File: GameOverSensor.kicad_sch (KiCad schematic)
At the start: 28 parts

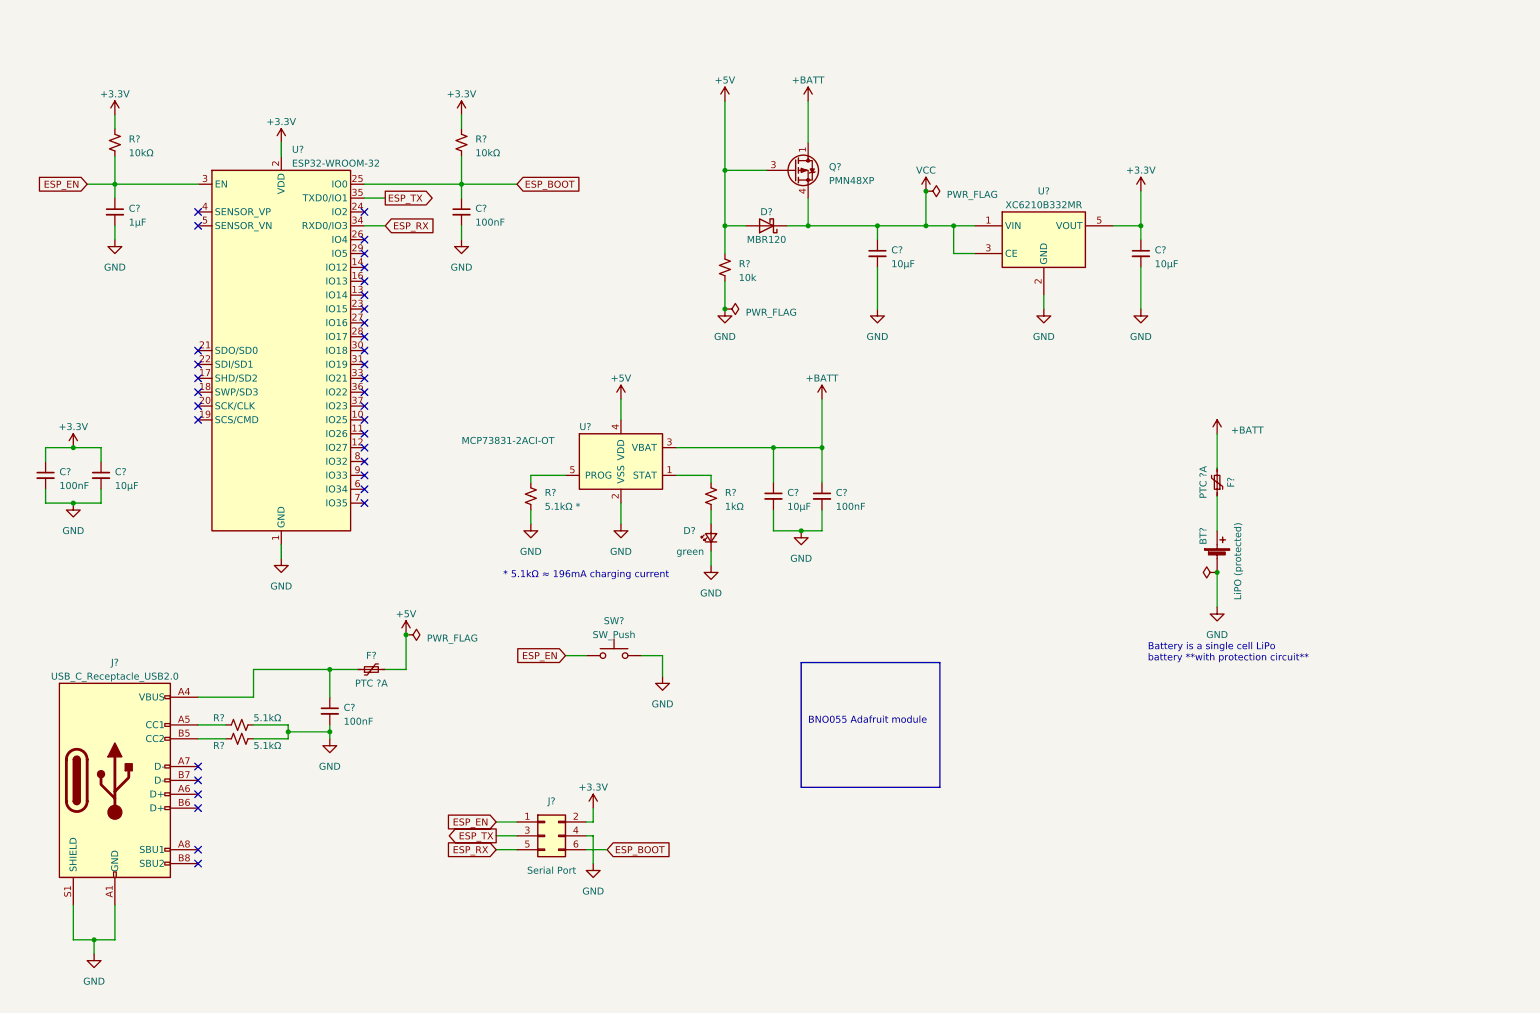
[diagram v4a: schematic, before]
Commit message: Reorganizes schematics a bit
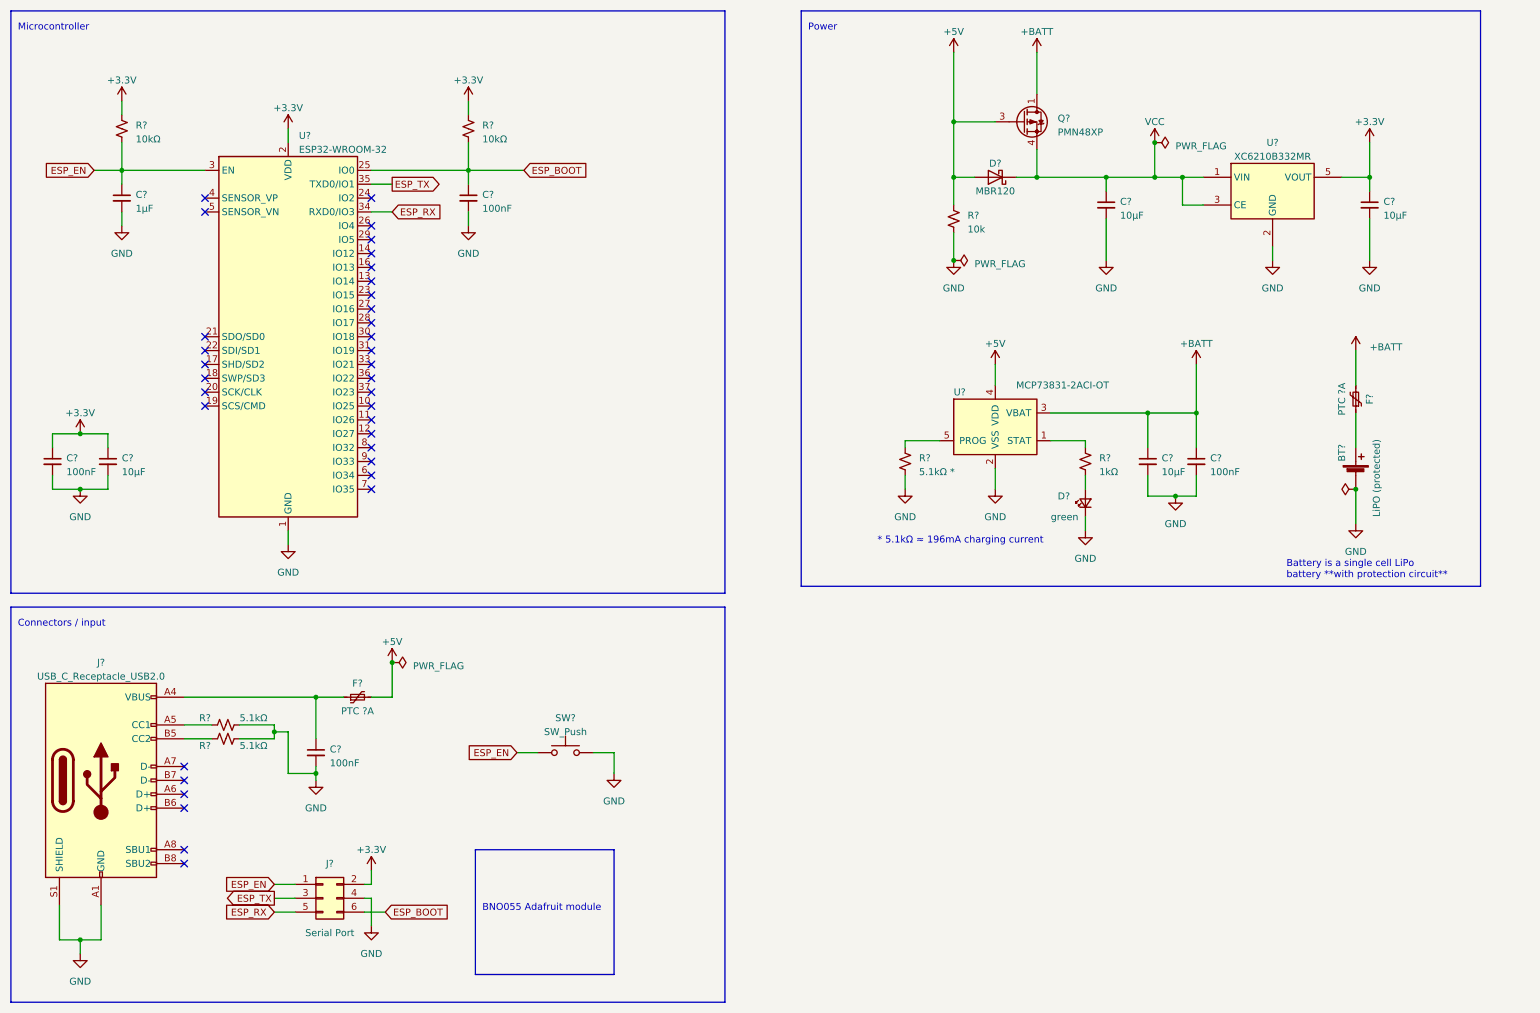
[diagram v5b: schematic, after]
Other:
- note added: "Connectors / input"
- note added: "Microcontroller"
- note added: "Power"
- company: (none) -> Dancelab Game Over
- title: (none) -> Game Over sensor
- moved on the sheet: BT?, C?, D?, F?, J?, Q?, R?, SW?, U?

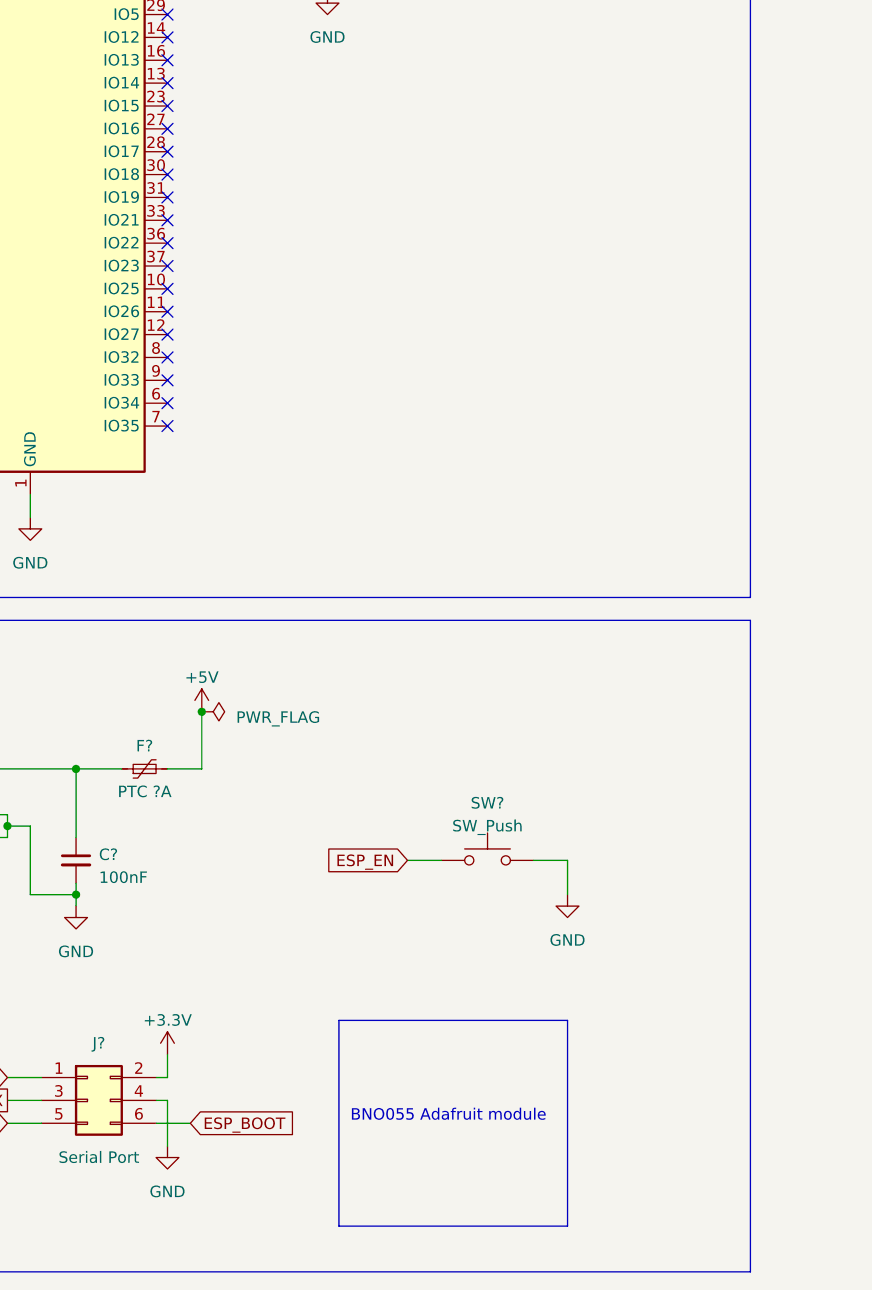
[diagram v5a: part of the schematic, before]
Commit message: Adds BON055 module symbol
We will use the Adafruit BON055 breakout board as we couldn't source the
BNO055 anywhere. This commit includes the schematic symbol but we still
need to make the footprint to be included in the PCB.
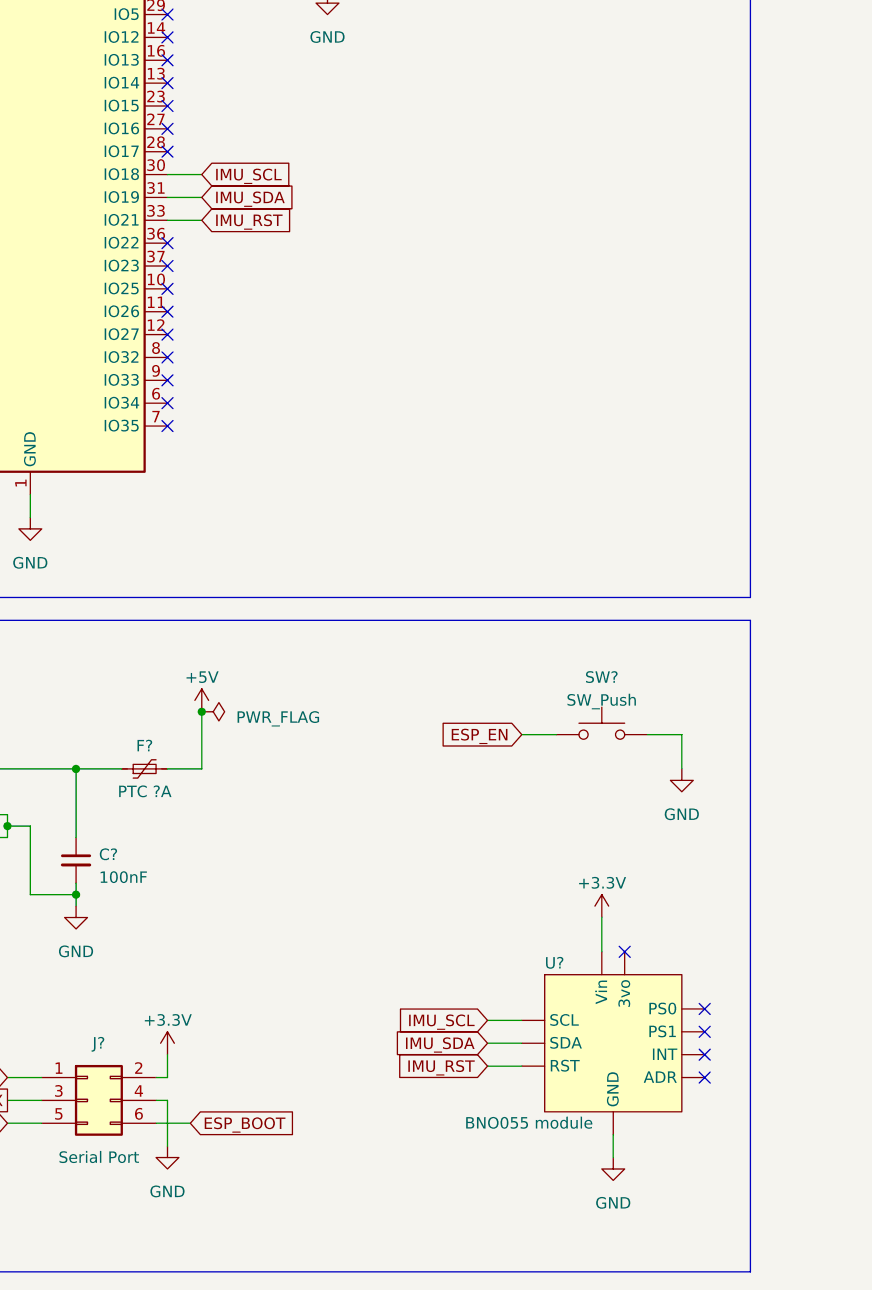
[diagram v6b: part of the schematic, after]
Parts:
- added U?: BNO055 module, symbol GameOver:Adafruit_BNO055_breakout
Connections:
- net +3V3: now also U?. (Vin)
- net GND: now also U?. (Vin)
- net IMU_SCL: now reaches U?.30 (IO18)
- net IMU_SCL: now also U?. (Vin)
- net IMU_SDA: now reaches U?.31 (IO19)
- net IMU_SDA: now also U?. (Vin)
- net IMU_RST: now reaches U?.33 (IO21)
- net IMU_RST: now also U?. (Vin)
- no-connect marks 35 -> 37
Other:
- note removed: "BNO055 Adafruit module"
- moved on the sheet: SW?

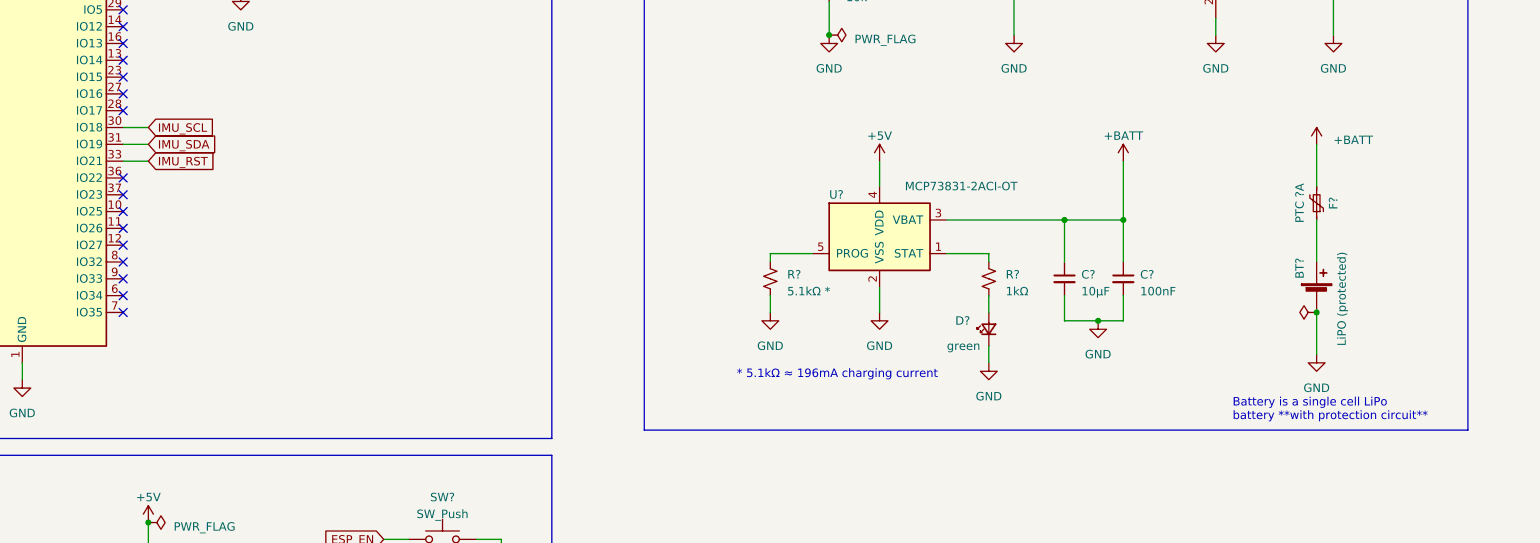
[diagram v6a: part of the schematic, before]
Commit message: Adds voltage divider to sense battery level
I decided to go with a simple voltage divider instead of a more complex
circuit that could be turned off because with two 100k resistors this
should mean a 21µA current when the battery is full (at 4.2V). This
seems like a good tradeoff to have a simpler circuit/BOM and layout
(since space is important here). Using two 100k might make the ADC a bit
noisy here, but this should be enough to have a good idea of the battery
level.

I'm using IO35 as that is in the first ADC block and block 2 is used by
wifi[1].

[1]: https://docs.micropython.org/en/latest/esp32/quickref.html#adc-analog-to-digital-conversion
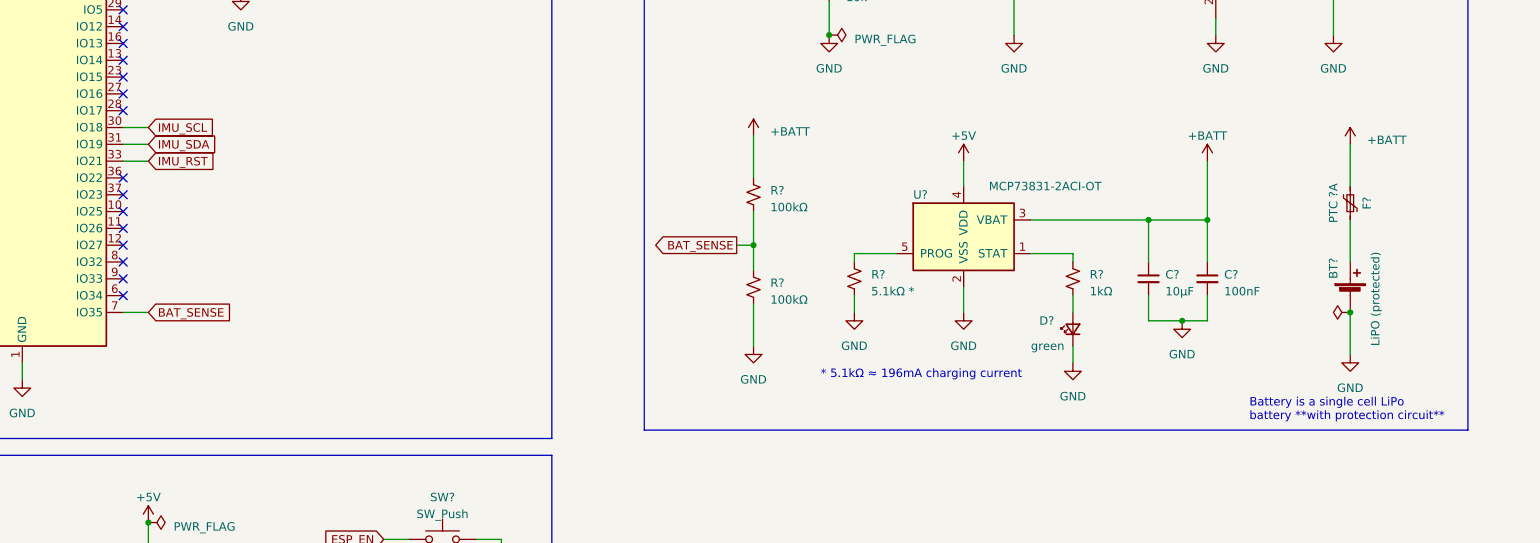
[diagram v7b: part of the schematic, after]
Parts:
- added R? (x2): 100kΩ, symbol Device:R_Small_US
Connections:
- net +BATT: now also R?.1
- net GND: now also R?.2
- net BAT_SENSE: now reaches U?.7 (IO35)
- net BAT_SENSE: now also R?.1, R?.2
- no-connect marks 37 -> 36
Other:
- moved on the sheet: BT?, C?, D?, F?, R?, U?
